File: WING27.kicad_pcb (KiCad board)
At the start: 2 copper layers, 60 parts, among them SW1 Kailh_CMI627301D60, SW10 Kailh_CMI627301D60, SW11 Kailh_CMI627301D60, SW12 Kailh_CMI627301D60, SW13 Kailh_CMI627301D60, SW14 Kailh_CMI627301D60, SW15 Kailh_CMI627301D60, SW16 Kailh_CMI627301D60, SW17 Kailh_CMI627301D60, SW18 Kailh_CMI627301D60, SW19 Kailh_CMI627301D60, SW2 Kailh_CMI627301D60, SW20 Kailh_CMI627301D60, SW21 Kailh_CMI627301D60, SW22 Kailh_CMI627301D60, SW23 Kailh_CMI627301D60, SW24 Kailh_CMI627301D60, SW25 Kailh_CMI627301D60, SW26 Kailh_CMI627301D60, SW27 Kailh_CMI627301D60, SW28 Kailh_CMI627301D60, SW29 Kailh_CMI627301D60, SW3 Kailh_CMI627301D60, SW30 Kailh_CMI627301D60, SW31 Kailh_CMI627301D60, SW32 Kailh_CMI627301D60, SW33 Kailh_CMI627301D60, SW34 Kailh_CMI627301D60, SW35 Kailh_CMI627301D60, SW36 Kailh_CMI627301D60, SW37 Kailh_CMI627301D60, SW38 Kailh_CMI627301D60, SW39 Kailh_CMI627301D60, SW4 Kailh_CMI627301D60, SW40 Kailh_CMI627301D60, SW41 Kailh_CMI627301D60, SW42 Kailh_CMI627301D60, SW43 Kailh_CMI627301D60, SW44 Kailh_CMI627301D60, SW45 Kailh_CMI627301D60, SW46 Kailh_CMI627301D60, SW47 Kailh_CMI627301D60, SW48 Kailh_CMI627301D60, SW49 Kailh_CMI627301D60, SW5 Kailh_CMI627301D60, SW50 Kailh_CMI627301D60, SW51 Kailh_CMI627301D60, SW52 Kailh_CMI627301D60, SW53 Kailh_CMI627301D60, SW54 Kailh_CMI627301D60, SW55 Kailh_CMI627301D60, SW56 Kailh_CMI627301D60, SW57 Kailh_CMI627301D60, SW58 Kailh_CMI627301D60, SW59 Kailh_CMI627301D60, SW6 Kailh_CMI627301D60, SW60 Kailh_CMI627301D60, SW7 Kailh_CMI627301D60, SW8 Kailh_CMI627301D60, SW9 Kailh_CMI627301D60

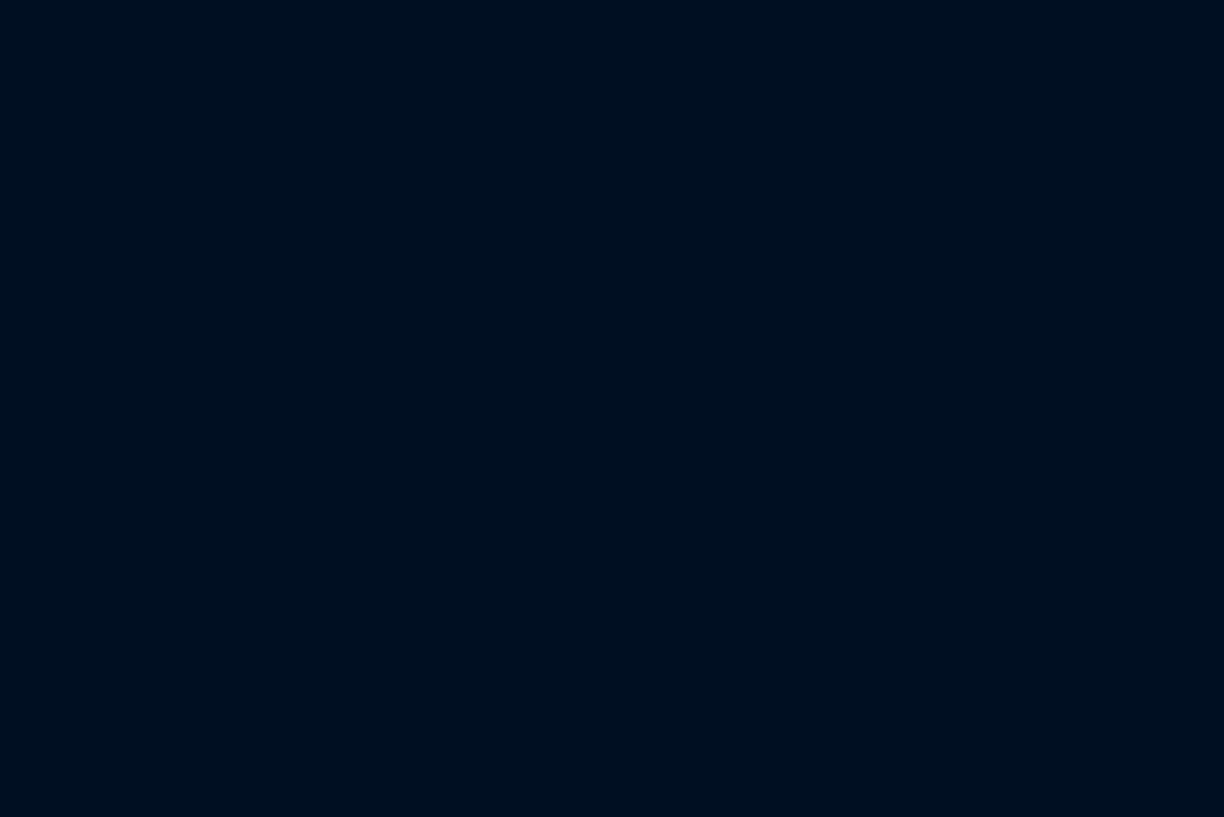
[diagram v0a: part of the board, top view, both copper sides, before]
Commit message: Complete WING27 electrical design and verified footprints before routing
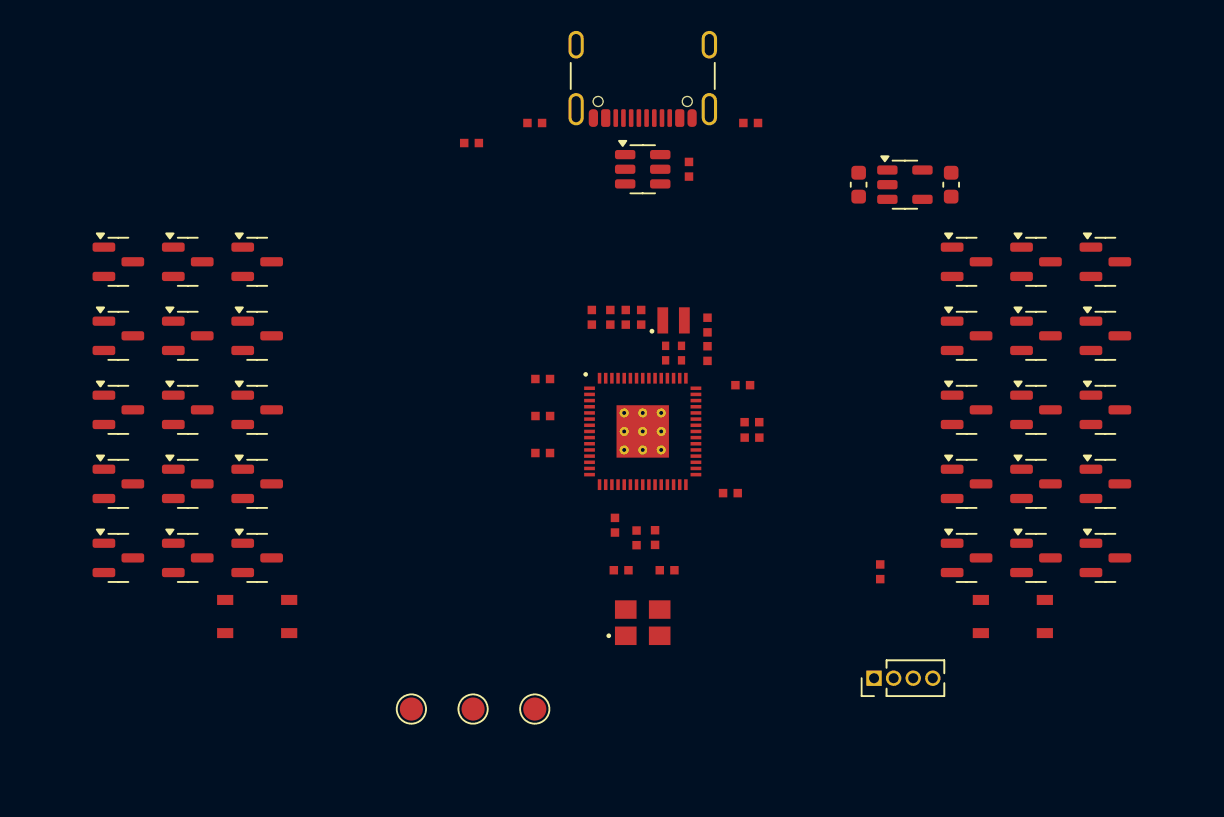
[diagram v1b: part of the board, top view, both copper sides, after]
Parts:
- added C1: 1u, WING27:C_0603_1608Metric, F.Cu at (138.0, 33.0)
- added C10: 4.7u, WING27:RPI_generic_capc1005x50, F.Cu at (124.8, 55.9)
- added C11: 100n, WING27:RPI_generic_capc1005x50, F.Cu at (131.1, 48.4)
- added C12: 100n, WING27:RPI_generic_capc1005x50, F.Cu at (121.9, 41.6)
- added C13: 100n, WING27:RPI_generic_capc1005x50, F.Cu at (117.5, 45.6)
- added C14: 100n, WING27:RPI_generic_capc1005x50, F.Cu at (131.1, 49.4)
- added C15: 100n, WING27:RPI_generic_capc1005x50, F.Cu at (117.5, 50.4)
- added C16: 100n, WING27:RPI_generic_capc1005x50, F.Cu at (129.7, 53.0)
- added C17: 100n, WING27:RPI_generic_capc1005x50, F.Cu at (130.5, 46.0)
- added C18: 100n, WING27:RPI_generic_capc1005x50, F.Cu at (122.2, 55.1)
- added C20: 100n, WING27:RPI_generic_capc1005x50, F.Cu at (120.7, 41.6)
- added C21: 100n, WING27:RPI_generic_capc1005x50, F.Cu at (127.0, 32.0)
- added C3: 15p, WING27:RPI_generic_capc1005x50, F.Cu at (122.6, 58.0)
- added C4: 15p, WING27:RPI_generic_capc1005x50, F.Cu at (125.6, 58.0)
- added C5: 1u, WING27:C_0603_1608Metric, F.Cu at (144.0, 33.0)
- added C6: 4.7u, WING27:RPI_generic_capc1005x50_wide, F.Cu at (126.0, 44.4)
- added C7: 4.7u, WING27:RPI_generic_capc1005x50_wide, F.Cu at (126.0, 43.5)
- added C8: 100n, WING27:RPI_generic_capc1005x50, F.Cu at (117.5, 48.0)
- added C9: 4.7u, WING27:RPI_generic_capc1005x50, F.Cu at (128.2, 44.0)
- added D1: BAV70, WING27:SOT-23, F.Cu at (90.0, 38.0)
- added D10: BAV70, WING27:SOT-23, F.Cu at (145.0, 42.8)
- added D11: BAV70, WING27:SOT-23, F.Cu at (149.5, 42.8)
- added D12: BAV70, WING27:SOT-23, F.Cu at (154.0, 42.8)
- added D13: BAV70, WING27:SOT-23, F.Cu at (90.0, 47.6)
- added D14: BAV70, WING27:SOT-23, F.Cu at (94.5, 47.6)
- added D15: BAV70, WING27:SOT-23, F.Cu at (99.0, 47.6)
- added D16: BAV70, WING27:SOT-23, F.Cu at (145.0, 47.6)
- added D17: BAV70, WING27:SOT-23, F.Cu at (149.5, 47.6)
- added D18: BAV70, WING27:SOT-23, F.Cu at (154.0, 47.6)
- added D19: BAV70, WING27:SOT-23, F.Cu at (90.0, 52.4)
- added D2: BAV70, WING27:SOT-23, F.Cu at (94.5, 38.0)
- added D20: BAV70, WING27:SOT-23, F.Cu at (94.5, 52.4)
- added D21: BAV70, WING27:SOT-23, F.Cu at (99.0, 52.4)
- added D22: BAV70, WING27:SOT-23, F.Cu at (145.0, 52.4)
- added D23: BAV70, WING27:SOT-23, F.Cu at (149.5, 52.4)
- added D24: BAV70, WING27:SOT-23, F.Cu at (154.0, 52.4)
- added D25: BAV70, WING27:SOT-23, F.Cu at (90.0, 57.2)
- added D26: BAV70, WING27:SOT-23, F.Cu at (94.5, 57.2)
- added D27: BAV70, WING27:SOT-23, F.Cu at (99.0, 57.2)
- added D28: BAV70, WING27:SOT-23, F.Cu at (145.0, 57.2)
- added D29: BAV70, WING27:SOT-23, F.Cu at (149.5, 57.2)
- added D3: BAV70, WING27:SOT-23, F.Cu at (99.0, 38.0)
- added D30: BAV70, WING27:SOT-23, F.Cu at (154.0, 57.2)
- added D4: BAV70, WING27:SOT-23, F.Cu at (145.0, 38.0)
- added D5: BAV70, WING27:SOT-23, F.Cu at (149.5, 38.0)
- added D6: BAV70, WING27:SOT-23, F.Cu at (154.0, 38.0)
- added D7: BAV70, WING27:SOT-23, F.Cu at (90.0, 42.8)
- added D8: BAV70, WING27:SOT-23, F.Cu at (94.5, 42.8)
- added D9: BAV70, WING27:SOT-23, F.Cu at (99.0, 42.8)
- added J1: USB4105-GF-A-060, WING27:USB_C_GCT_USB4105_GF_A060_JLC, F.Cu at (124.0, 25.0)
- added J2: SWD, WING27:PinHeader_1x04_P1.27mm_Vertical, F.Cu at (139.0, 65.0)
- added L1: 3.3uH, WING27:RPI_abracon_aota-b201610s3r3-101-t, F.Cu at (126.0, 41.8)
- added R2: 1k, WING27:RPI_generic_resc1005x35, F.Cu at (123.6, 55.9)
- added R20: 5.1k, WING27:RPI_generic_resc1005x35, F.Cu at (117.0, 29.0)
- added R21: 5.1k, WING27:RPI_generic_resc1005x35, F.Cu at (131.0, 29.0)
- added R3: 33, WING27:RPI_generic_resc1005x35, F.Cu at (128.2, 42.1)
- added R4: 1k, WING27:RPI_generic_resc1005x35, F.Cu at (139.4, 58.1)
- added R6: 1k, WING27:RPI_generic_resc1005x35, F.Cu at (112.9, 30.3)
- added R7: 27, WING27:RPI_generic_resc1005x35, F.Cu at (122.9, 41.6)
- added R8: 27, WING27:RPI_generic_resc1005x35, F.Cu at (123.9, 41.6)
- added SW61: BOOTSEL, WING27:RPI_wurthelek_434133025816, F.Cu at (99.0, 61.0)
- added SW62: RESET, WING27:RPI_wurthelek_434133025816, F.Cu at (148.0, 61.0)
- added TP1: VBUS, WING27:TestPoint_Pad_D1.5mm, F.Cu at (109.0, 67.0)
- added TP2: EXP_GPIO17_3V3, WING27:TestPoint_Pad_D1.5mm, F.Cu at (113.0, 67.0)
- added TP3: GND, WING27:TestPoint_Pad_D1.5mm, F.Cu at (117.0, 67.0)
- added U1: RP2354A, WING27:RPI_rpi_rp2350a_vias, F.Cu at (124.0, 49.0)
- added U2: AP2112K-3.3TRG1, WING27:SOT-23-5, F.Cu at (141.0, 33.0)
- added U3: USBLC6-2SC6, WING27:SOT-23-6, F.Cu at (124.0, 32.0)
- added X1: 12MHz, WING27:RPI_generic_xtalcc320x250x80-4, F.Cu at (124.0, 61.4)
- SW1, SW10, SW11, SW12, SW13, SW14, SW15, SW16, SW17, SW18, SW19, SW2, SW20, SW21, SW22, SW23, SW24, SW25, SW26, SW27, SW28, SW29, SW3, SW30, SW31, SW32, SW33, SW34, SW35, SW36, SW37, SW38, SW39, SW4, SW40, SW41, SW42, SW43, SW44, SW45, SW46, SW47, SW48, SW49, SW5, SW50, SW51, SW52, SW53, SW54, SW55, SW56, SW57, SW58, SW59, SW6, SW60, SW7, SW8, SW9: value Kailh_CMI627301D60 -> CMI627301D60
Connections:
- SW1 pad 1: unconnected-(SW1-Pad1) -> COL0
- SW1 pad 2: unconnected-(SW1-Pad2) -> /KEY_L1_1
- SW10 pad 1: unconnected-(SW10-Pad1) -> COL3
- SW10 pad 2: unconnected-(SW10-Pad2) -> /KEY_L2_4
- SW11 pad 1: unconnected-(SW11-Pad1) -> COL4
- SW11 pad 2: unconnected-(SW11-Pad2) -> /KEY_L2_5
- SW12 pad 1: unconnected-(SW12-Pad1) -> COL5
- SW12 pad 2: unconnected-(SW12-Pad2) -> /KEY_L2_6
- SW13 pad 1: unconnected-(SW13-Pad1) -> COL0
- SW13 pad 2: unconnected-(SW13-Pad2) -> /KEY_L3_1
- SW14 pad 1: unconnected-(SW14-Pad1) -> COL1
- SW14 pad 2: unconnected-(SW14-Pad2) -> /KEY_L3_2
- SW15 pad 1: unconnected-(SW15-Pad1) -> COL2
- SW15 pad 2: unconnected-(SW15-Pad2) -> /KEY_L3_3
- SW16 pad 1: unconnected-(SW16-Pad1) -> COL3
- SW16 pad 2: unconnected-(SW16-Pad2) -> /KEY_L3_4
- SW17 pad 1: unconnected-(SW17-Pad1) -> COL4
- SW17 pad 2: unconnected-(SW17-Pad2) -> /KEY_L3_5
- SW18 pad 1: unconnected-(SW18-Pad1) -> COL5
- SW18 pad 2: unconnected-(SW18-Pad2) -> /KEY_L3_6
- SW19 pad 1: unconnected-(SW19-Pad1) -> COL0
- SW19 pad 2: unconnected-(SW19-Pad2) -> /KEY_L4_1
- SW2 pad 1: unconnected-(SW2-Pad1) -> COL1
- SW2 pad 2: unconnected-(SW2-Pad2) -> /KEY_L1_2
- SW20 pad 1: unconnected-(SW20-Pad1) -> COL1
- SW20 pad 2: unconnected-(SW20-Pad2) -> /KEY_L4_2
- SW21 pad 1: unconnected-(SW21-Pad1) -> COL2
- SW21 pad 2: unconnected-(SW21-Pad2) -> /KEY_L4_3
- SW22 pad 1: unconnected-(SW22-Pad1) -> COL3
- SW22 pad 2: unconnected-(SW22-Pad2) -> /KEY_L4_4
- SW23 pad 1: unconnected-(SW23-Pad1) -> COL4
- SW23 pad 2: unconnected-(SW23-Pad2) -> /KEY_L4_5
- SW24 pad 1: unconnected-(SW24-Pad1) -> COL5
- SW24 pad 2: unconnected-(SW24-Pad2) -> /KEY_L4_6
- SW25 pad 1: unconnected-(SW25-Pad1) -> COL0
- SW25 pad 2: unconnected-(SW25-Pad2) -> /KEY_L5_1
- SW26 pad 1: unconnected-(SW26-Pad1) -> COL1
- SW26 pad 2: unconnected-(SW26-Pad2) -> /KEY_L5_2
- SW27 pad 1: unconnected-(SW27-Pad1) -> COL2
- SW27 pad 2: unconnected-(SW27-Pad2) -> /KEY_L5_3
- SW28 pad 1: unconnected-(SW28-Pad1) -> COL3
- SW28 pad 2: unconnected-(SW28-Pad2) -> /KEY_L5_4
- SW29 pad 1: unconnected-(SW29-Pad1) -> COL4
- SW29 pad 2: unconnected-(SW29-Pad2) -> /KEY_L5_5
- SW3 pad 1: unconnected-(SW3-Pad1) -> COL2
- SW3 pad 2: unconnected-(SW3-Pad2) -> /KEY_L1_3
- SW30 pad 1: unconnected-(SW30-Pad1) -> COL5
- SW30 pad 2: unconnected-(SW30-Pad2) -> /KEY_L5_6
- SW31 pad 1: unconnected-(SW31-Pad1) -> COL6
- SW31 pad 2: unconnected-(SW31-Pad2) -> /KEY_R1_1
- SW32 pad 1: unconnected-(SW32-Pad1) -> COL7
- SW32 pad 2: unconnected-(SW32-Pad2) -> /KEY_R1_2
- SW33 pad 1: unconnected-(SW33-Pad1) -> COL8
- SW33 pad 2: unconnected-(SW33-Pad2) -> /KEY_R1_3
- SW34 pad 1: unconnected-(SW34-Pad1) -> COL9
- SW34 pad 2: unconnected-(SW34-Pad2) -> /KEY_R1_4
- SW35 pad 1: unconnected-(SW35-Pad1) -> COL10
- SW35 pad 2: unconnected-(SW35-Pad2) -> /KEY_R1_5
- SW36 pad 1: unconnected-(SW36-Pad1) -> COL11
- SW36 pad 2: unconnected-(SW36-Pad2) -> /KEY_R1_6
- SW37 pad 1: unconnected-(SW37-Pad1) -> COL10
- SW37 pad 2: unconnected-(SW37-Pad2) -> /KEY_R1_7
- SW38 pad 1: unconnected-(SW38-Pad1) -> COL6
- SW38 pad 2: unconnected-(SW38-Pad2) -> /KEY_R2_1
- SW39 pad 1: unconnected-(SW39-Pad1) -> COL7
- SW39 pad 2: unconnected-(SW39-Pad2) -> /KEY_R2_2
- SW4 pad 1: unconnected-(SW4-Pad1) -> COL3
- SW4 pad 2: unconnected-(SW4-Pad2) -> /KEY_L1_4
- SW40 pad 1: unconnected-(SW40-Pad1) -> COL8
- SW40 pad 2: unconnected-(SW40-Pad2) -> /KEY_R2_3
- SW41 pad 1: unconnected-(SW41-Pad1) -> COL9
- SW41 pad 2: unconnected-(SW41-Pad2) -> /KEY_R2_4
- SW42 pad 1: unconnected-(SW42-Pad1) -> COL10
- SW42 pad 2: unconnected-(SW42-Pad2) -> /KEY_R2_5
- SW43 pad 1: unconnected-(SW43-Pad1) -> COL11
- SW43 pad 2: unconnected-(SW43-Pad2) -> /KEY_R2_6
- SW44 pad 1: unconnected-(SW44-Pad1) -> COL6
- SW44 pad 2: unconnected-(SW44-Pad2) -> /KEY_R3_1
- SW45 pad 1: unconnected-(SW45-Pad1) -> COL7
- SW45 pad 2: unconnected-(SW45-Pad2) -> /KEY_R3_2
- SW46 pad 1: unconnected-(SW46-Pad1) -> COL8
- SW46 pad 2: unconnected-(SW46-Pad2) -> /KEY_R3_3
- SW47 pad 1: unconnected-(SW47-Pad1) -> COL9
- SW47 pad 2: unconnected-(SW47-Pad2) -> /KEY_R3_4
- SW48 pad 1: unconnected-(SW48-Pad1) -> COL11
- SW48 pad 2: unconnected-(SW48-Pad2) -> /KEY_R3_5
- SW49 pad 1: unconnected-(SW49-Pad1) -> COL6
- SW49 pad 2: unconnected-(SW49-Pad2) -> /KEY_R4_1
- SW5 pad 1: unconnected-(SW5-Pad1) -> COL4
- SW5 pad 2: unconnected-(SW5-Pad2) -> /KEY_L1_5
- SW50 pad 1: unconnected-(SW50-Pad1) -> COL7
- SW50 pad 2: unconnected-(SW50-Pad2) -> /KEY_R4_2
- SW51 pad 1: unconnected-(SW51-Pad1) -> COL8
- SW51 pad 2: unconnected-(SW51-Pad2) -> /KEY_R4_3
- SW52 pad 1: unconnected-(SW52-Pad1) -> COL9
- SW52 pad 2: unconnected-(SW52-Pad2) -> /KEY_R4_4
- SW53 pad 1: unconnected-(SW53-Pad1) -> COL10
- SW53 pad 2: unconnected-(SW53-Pad2) -> /KEY_R4_5
- SW54 pad 1: unconnected-(SW54-Pad1) -> COL11
- SW54 pad 2: unconnected-(SW54-Pad2) -> /KEY_R4_6
- SW55 pad 1: unconnected-(SW55-Pad1) -> COL6
- SW55 pad 2: unconnected-(SW55-Pad2) -> /KEY_R5_1
- SW56 pad 1: unconnected-(SW56-Pad1) -> COL7
- SW56 pad 2: unconnected-(SW56-Pad2) -> /KEY_R5_2
- SW57 pad 1: unconnected-(SW57-Pad1) -> COL8
- SW57 pad 2: unconnected-(SW57-Pad2) -> /KEY_R5_3
- SW58 pad 1: unconnected-(SW58-Pad1) -> COL9
- SW58 pad 2: unconnected-(SW58-Pad2) -> /KEY_R5_4
- SW59 pad 1: unconnected-(SW59-Pad1) -> COL10
- SW59 pad 2: unconnected-(SW59-Pad2) -> /KEY_R5_5
- SW6 pad 1: unconnected-(SW6-Pad1) -> COL5
- SW6 pad 2: unconnected-(SW6-Pad2) -> /KEY_L1_6
- SW60 pad 1: unconnected-(SW60-Pad1) -> COL11
- SW60 pad 2: unconnected-(SW60-Pad2) -> /KEY_R5_6
- SW7 pad 1: unconnected-(SW7-Pad1) -> COL0
- SW7 pad 2: unconnected-(SW7-Pad2) -> /KEY_L2_1
- SW8 pad 1: unconnected-(SW8-Pad1) -> COL1
- SW8 pad 2: unconnected-(SW8-Pad2) -> /KEY_L2_2
- SW9 pad 1: unconnected-(SW9-Pad1) -> COL2
- SW9 pad 2: unconnected-(SW9-Pad2) -> /KEY_L2_3
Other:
- board text added: "KEY CENTRES LOCKED / ELECTRICAL NETS COMPLETE / UNROUTED / outline & stackup provisional"
- board text removed: "KEY CENTRES LOCKED / matrix, MCU, USB-C, LED, outline and thickness pending"

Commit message: Refine WING27 schematics, SWD connector, panel overlay and mounting
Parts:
- added H1: M2 clearance 2.2mm, WING27:MountingHole_2.2mm_M2, F.Cu at (23.0, 75.0)
- added H2: M2 clearance 2.2mm, WING27:MountingHole_2.2mm_M2, F.Cu at (23.0, 23.0)
- added H3: M2 clearance 2.2mm, WING27:MountingHole_2.2mm_M2, F.Cu at (225.0, 75.0)
- added H4: M2 clearance 2.2mm, WING27:MountingHole_2.2mm_M2, F.Cu at (225.0, 23.0)
- added R22: 100, WING27:RPI_generic_resc1005x35, F.Cu at (123.9, 44.1)
- added R23: 100, WING27:RPI_generic_resc1005x35, F.Cu at (122.6, 44.1)
- J2: value SWD -> BM03B-SRSS-TB; footprint WING27:PinHeader_1x04_P1.27mm_Vertical -> WING27:JST_SH_BM03B-SRSS-TB_1x03-1MP_P1.00mm_Vertical
- moved SW61 59.4 mm to (149.0, 29.0), turned to 180 degrees
- moved SW62 57.7 mm to (100.0, 29.0), turned to 180 degrees
- moved C5 51.2 mm to (104.0, 65.0), turned to -90 degrees
- moved J1 48.0 mm to (124.0, 73.0), turned to 0 degrees
- moved TP1 46.9 mm to (139.0, 31.0), turned to 180 degrees
- moved U2 46.7 mm to (107.0, 65.0), turned to 180 degrees
- moved J2 43.9 mm to (109.0, 33.0), turned to -90 degrees
- moved R6 43.5 mm to (135.1, 67.7), turned to 180 degrees
- moved C1 42.5 mm to (110.0, 65.0), turned to -90 degrees
- moved R20 42.4 mm to (131.0, 69.0), turned to 180 degrees
- moved R21 42.4 mm to (117.0, 69.0), turned to 180 degrees
- moved TP2 42.2 mm to (135.0, 31.0), turned to 180 degrees
- moved TP3 38.6 mm to (131.0, 31.0), turned to 180 degrees
- moved R4 35.8 mm to (108.6, 39.9), turned to 90 degrees
- moved C21 34.5 mm to (121.0, 66.0), turned to -90 degrees
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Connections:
- J2 pad 1: /Controller/+3V3 -> /Controller/SWCLK
- J2 pad 2: /Controller/SWDIO -> /Controller/GND
- J2 pad 3: /Controller/GND -> /Controller/SWDIO
- U1 pad 24: /Controller/SWCLK -> /Controller/SWCLK_MCU
- U1 pad 25: /Controller/SWDIO -> /Controller/SWDIO_MCU

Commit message: Split keyboard GPIO banks and refine basic parts and SWD options
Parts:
- added J3: SWD 2.54 DNP, WING27:PinHeader_1x03_P2.54mm_Vertical, F.Cu at (112.0, 39.0)
- C5: value 1u -> 4.7u
- SW61, SW62: footprint WING27:RPI_wurthelek_434133025816 -> WING27:SW_SPST_TS-1088-AR02016
- U2: value AP2112K-3.3TRG1 -> XC6206P332MR-G; footprint WING27:SOT-23-5 -> WING27:XC6206_SOT23_Torex_Reference
- turned D10 to 180 degrees
- turned D11 to 180 degrees
- turned D12 to 180 degrees
- turned D16 to 180 degrees
- turned D17 to 180 degrees
- turned D18 to 180 degrees
- turned D22 to 180 degrees
- turned D23 to 180 degrees
- turned D24 to 180 degrees
- turned D28 to 180 degrees
- turned D29 to 180 degrees
- turned D30 to 180 degrees
- turned D4 to 180 degrees
- turned D5 to 180 degrees
- turned D6 to 180 degrees
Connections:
- D1 pad 3: ROW0 -> ROW_L0
- D10 pad 3: ROW1 -> ROW_R1
- D11 pad 3: ROW1 -> ROW_R1
- D12 pad 3: ROW1 -> ROW_R1
- D13 pad 3: ROW2 -> ROW_L2
- D14 pad 3: ROW2 -> ROW_L2
- D15 pad 3: ROW2 -> ROW_L2
- D16 pad 3: ROW2 -> ROW_R2
- D17 pad 3: ROW2 -> ROW_R2
- D18 pad 3: ROW2 -> ROW_R2
- D19 pad 3: ROW3 -> ROW_L3
- D2 pad 3: ROW0 -> ROW_L0
- D20 pad 3: ROW3 -> ROW_L3
- D21 pad 3: ROW3 -> ROW_L3
- D22 pad 3: ROW3 -> ROW_R3
- D23 pad 3: ROW3 -> ROW_R3
- D24 pad 3: ROW3 -> ROW_R3
- D25 pad 3: ROW4 -> ROW_L4
- D26 pad 3: ROW4 -> ROW_L4
- D27 pad 3: ROW4 -> ROW_L4
- D28 pad 3: ROW4 -> ROW_R4
- D29 pad 3: ROW4 -> ROW_R4
- D3 pad 3: ROW0 -> ROW_L0
- D30 pad 3: ROW4 -> ROW_R4
- D4 pad 3: ROW0 -> ROW_R0
- D5 pad 3: ROW0 -> ROW_R0
- D6 pad 3: ROW0 -> ROW_R0
- D7 pad 3: ROW1 -> ROW_L1
- D8 pad 3: ROW1 -> ROW_L1
- D9 pad 3: ROW1 -> ROW_L1
- SW61 pad 2: /Controller/GND -> /Controller/BOOT_SWITCH
- SW62 pad 2: /Controller/RUN_SWITCH -> /Controller/RUN
- U1 pad 16: ROW0 -> unconnected-(U1-GPIO12-Pad16)
- U1 pad 17: ROW1 -> unconnected-(U1-GPIO13-Pad17)
- U1 pad 18: ROW2 -> unconnected-(U1-GPIO14-Pad18)
- U1 pad 19: ROW3 -> unconnected-(U1-GPIO15-Pad19)
- U1 pad 2: COL0 -> ROW_R0
- U1 pad 27: ROW4 -> unconnected-(U1-GPIO16-Pad27)
- U1 pad 3: COL1 -> ROW_R1
- U1 pad 31: unconnected-(U1-GPIO19-Pad31) -> COL0
- U1 pad 32: unconnected-(U1-GPIO20-Pad32) -> COL1
- U1 pad 33: unconnected-(U1-GPIO21-Pad33) -> COL2
- U1 pad 34: unconnected-(U1-GPIO22-Pad34) -> COL3
- U1 pad 35: unconnected-(U1-GPIO23-Pad35) -> COL4
- U1 pad 36: unconnected-(U1-GPIO24-Pad36) -> COL5
- U1 pad 37: unconnected-(U1-GPIO25-Pad37) -> ROW_L0
- U1 pad 4: COL2 -> ROW_R2
- U1 pad 40: unconnected-(U1-GPIO26_ADC0-Pad40) -> ROW_L1
- U1 pad 41: unconnected-(U1-GPIO27_ADC1-Pad41) -> ROW_L2
- U1 pad 42: unconnected-(U1-GPIO28_ADC2-Pad42) -> ROW_L3
- U1 pad 43: unconnected-(U1-GPIO29_ADC3-Pad43) -> ROW_L4
- U1 pad 5: COL3 -> ROW_R3
- U1 pad 7: COL4 -> ROW_R4
- U1 pad 8: COL5 -> unconnected-(U1-GPIO5-Pad8)
- U2 pad 1: /Controller/VBUS -> /Controller/GND
- U2 pad 2: /Controller/GND -> /Controller/+3V3
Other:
- board text added: "1"
- board text added: "CLK"
- board text added: "DIO"
- board text added: "GND"
- board text added: "J3 SWD DNP"

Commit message: Add side LEDs and preserve verified official core routing
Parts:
- added C22: 100n, WING27:RPI_generic_capc1005x50, F.Cu at (76.5, 34.8)
- added C23: 100n, WING27:RPI_generic_capc1005x50, F.Cu at (76.5, 44.8)
- added C24: 100n, WING27:RPI_generic_capc1005x50, F.Cu at (76.5, 54.8)
- added C25: 100n, WING27:RPI_generic_capc1005x50, F.Cu at (76.5, 64.8)
- added C26: 100n, WING27:RPI_generic_capc1005x50, F.Cu at (25.5, 64.8)
- added C27: 100n, WING27:RPI_generic_capc1005x50, F.Cu at (25.5, 54.8)
- added C28: 100n, WING27:RPI_generic_capc1005x50, F.Cu at (25.5, 44.8)
- added C29: 100n, WING27:RPI_generic_capc1005x50, F.Cu at (25.5, 34.8)
- added C30: 100n, WING27:RPI_generic_capc1005x50, F.Cu at (169.5, 34.8)
- added C31: 100n, WING27:RPI_generic_capc1005x50, F.Cu at (169.5, 44.8)
- added C32: 100n, WING27:RPI_generic_capc1005x50, F.Cu at (169.5, 54.8)
- added C33: 100n, WING27:RPI_generic_capc1005x50, F.Cu at (169.5, 64.8)
- added C34: 100n, WING27:RPI_generic_capc1005x50, F.Cu at (222.5, 64.8)
- added C35: 100n, WING27:RPI_generic_capc1005x50, F.Cu at (222.5, 54.8)
- added C36: 100n, WING27:RPI_generic_capc1005x50, F.Cu at (222.5, 44.8)
- added C37: 100n, WING27:RPI_generic_capc1005x50, F.Cu at (222.5, 34.8)
- added D31: WS2812B-4020-V6, WING27:WS2812B_4020_V6_LCSC_Reference, F.Cu at (79.5, 34.0)
- added D32: WS2812B-4020-V6, WING27:WS2812B_4020_V6_LCSC_Reference, F.Cu at (79.5, 44.0)
- added D33: WS2812B-4020-V6, WING27:WS2812B_4020_V6_LCSC_Reference, F.Cu at (79.5, 54.0)
- added D34: WS2812B-4020-V6, WING27:WS2812B_4020_V6_LCSC_Reference, F.Cu at (79.5, 64.0)
- added D35: WS2812B-4020-V6, WING27:WS2812B_4020_V6_LCSC_Reference, F.Cu at (22.5, 64.0)
- added D36: WS2812B-4020-V6, WING27:WS2812B_4020_V6_LCSC_Reference, F.Cu at (22.5, 54.0)
- added D37: WS2812B-4020-V6, WING27:WS2812B_4020_V6_LCSC_Reference, F.Cu at (22.5, 44.0)
- added D38: WS2812B-4020-V6, WING27:WS2812B_4020_V6_LCSC_Reference, F.Cu at (22.5, 34.0)
- added D39: WS2812B-4020-V6, WING27:WS2812B_4020_V6_LCSC_Reference, F.Cu at (166.5, 34.0)
- added D40: WS2812B-4020-V6, WING27:WS2812B_4020_V6_LCSC_Reference, F.Cu at (166.5, 44.0)
- added D41: WS2812B-4020-V6, WING27:WS2812B_4020_V6_LCSC_Reference, F.Cu at (166.5, 54.0)
- added D42: WS2812B-4020-V6, WING27:WS2812B_4020_V6_LCSC_Reference, F.Cu at (166.5, 64.0)
- added D43: WS2812B-4020-V6, WING27:WS2812B_4020_V6_LCSC_Reference, F.Cu at (225.5, 64.0)
- added D44: WS2812B-4020-V6, WING27:WS2812B_4020_V6_LCSC_Reference, F.Cu at (225.5, 54.0)
- added D45: WS2812B-4020-V6, WING27:WS2812B_4020_V6_LCSC_Reference, F.Cu at (225.5, 44.0)
- added D46: WS2812B-4020-V6, WING27:WS2812B_4020_V6_LCSC_Reference, F.Cu at (225.5, 34.0)
- added JP1: OPEN, WING27:SolderJumper-2_P1.3mm_Open_Pad1.0x1.5mm, B.Cu at (77.5, 34.0)
- added JP10: OPEN, WING27:SolderJumper-2_P1.3mm_Open_Pad1.0x1.5mm, B.Cu at (168.5, 44.0)
- added JP11: OPEN, WING27:SolderJumper-2_P1.3mm_Open_Pad1.0x1.5mm, B.Cu at (168.5, 54.0)
- added JP12: OPEN, WING27:SolderJumper-2_P1.3mm_Open_Pad1.0x1.5mm, B.Cu at (168.5, 64.0)
- added JP13: OPEN, WING27:SolderJumper-2_P1.3mm_Open_Pad1.0x1.5mm, B.Cu at (223.5, 64.0)
- added JP14: OPEN, WING27:SolderJumper-2_P1.3mm_Open_Pad1.0x1.5mm, B.Cu at (223.5, 54.0)
- added JP15: OPEN, WING27:SolderJumper-2_P1.3mm_Open_Pad1.0x1.5mm, B.Cu at (223.5, 44.0)
- added JP16: OPEN, WING27:SolderJumper-2_P1.3mm_Open_Pad1.0x1.5mm, B.Cu at (223.5, 34.0)
- added JP2: OPEN, WING27:SolderJumper-2_P1.3mm_Open_Pad1.0x1.5mm, B.Cu at (77.5, 44.0)
- added JP3: OPEN, WING27:SolderJumper-2_P1.3mm_Open_Pad1.0x1.5mm, B.Cu at (77.5, 54.0)
- added JP4: OPEN, WING27:SolderJumper-2_P1.3mm_Open_Pad1.0x1.5mm, B.Cu at (77.5, 64.0)
- added JP5: OPEN, WING27:SolderJumper-2_P1.3mm_Open_Pad1.0x1.5mm, B.Cu at (24.5, 64.0)
- added JP6: OPEN, WING27:SolderJumper-2_P1.3mm_Open_Pad1.0x1.5mm, B.Cu at (24.5, 54.0)
- added JP7: OPEN, WING27:SolderJumper-2_P1.3mm_Open_Pad1.0x1.5mm, B.Cu at (24.5, 44.0)
- added JP8: OPEN, WING27:SolderJumper-2_P1.3mm_Open_Pad1.0x1.5mm, B.Cu at (24.5, 34.0)
- added JP9: OPEN, WING27:SolderJumper-2_P1.3mm_Open_Pad1.0x1.5mm, B.Cu at (168.5, 34.0)
- added R24: 100, WING27:RPI_generic_resc1005x35, F.Cu at (135.0, 34.0)
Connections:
- net /Controller/EXP_GPIO17_3V3 renamed EXP_GPIO17_3V3
- net /Controller/GND renamed GND
- net /Controller/VBUS renamed VBUS
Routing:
- net /Controller/+3V3: track 0.00 -> 27.0 mm
- net /Controller/+1V1: track 0.00 -> 24.1 mm, vias 0 -> 9
- net /Controller/XIN: track 0.00 -> 10.9 mm
- net GND: track 0.00 -> 10.6 mm, vias 0 -> 18
- net /Controller/XTAL_OUT: track 0.00 -> 5.42 mm
- net /Controller/VREG_AVDD: track 0.00 -> 3.53 mm
- net /Controller/XOUT: track 0.00 -> 2.96 mm
- added copper zone on F.Cu, net /Controller/+1V1
- added copper zone on F.Cu, net /Controller/+3V3
- added copper zone on F.Cu, net /Controller/VREG_LX
- added copper zone on B.Cu, net GND
- added copper zone on F.Cu, net GND
